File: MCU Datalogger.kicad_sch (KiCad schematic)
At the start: 0 parts

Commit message: Have added required symbols to the schematic sheets.
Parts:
- added BT?: Battery, symbol Device:Battery
- added C? (x5): C, symbol Device:C
- added D? (x2): LED, symbol Device:LED
- added H? (x4): MountingHole, symbol Mechanical:MountingHole
- added R? (x7): R, symbol Device:R
- added U?: DS1337S_, DS1337S_:SOIC127P600X175-8N, symbol DS1337S_:DS1337S_
- added U? (x2): 24LC1025, symbol Memory_EEPROM:24LC1025
- added U?: ATMEGA328P-AU, ATMEGA328P-AU:QFP80P900X900X120-32N, symbol ATMEGA328P-AU:ATMEGA328P-AU
- added Y? (x2): Crystal, symbol Device:Crystal
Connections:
- new net: U?.21 (GND), U?.3 (GND), U?.5 (GND)
- new net: U?.4 (VCC), U?.6 (VCC)
- no-connect marks 0 -> 1
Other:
- added sheet Connectors (connectors.kicad_sch)

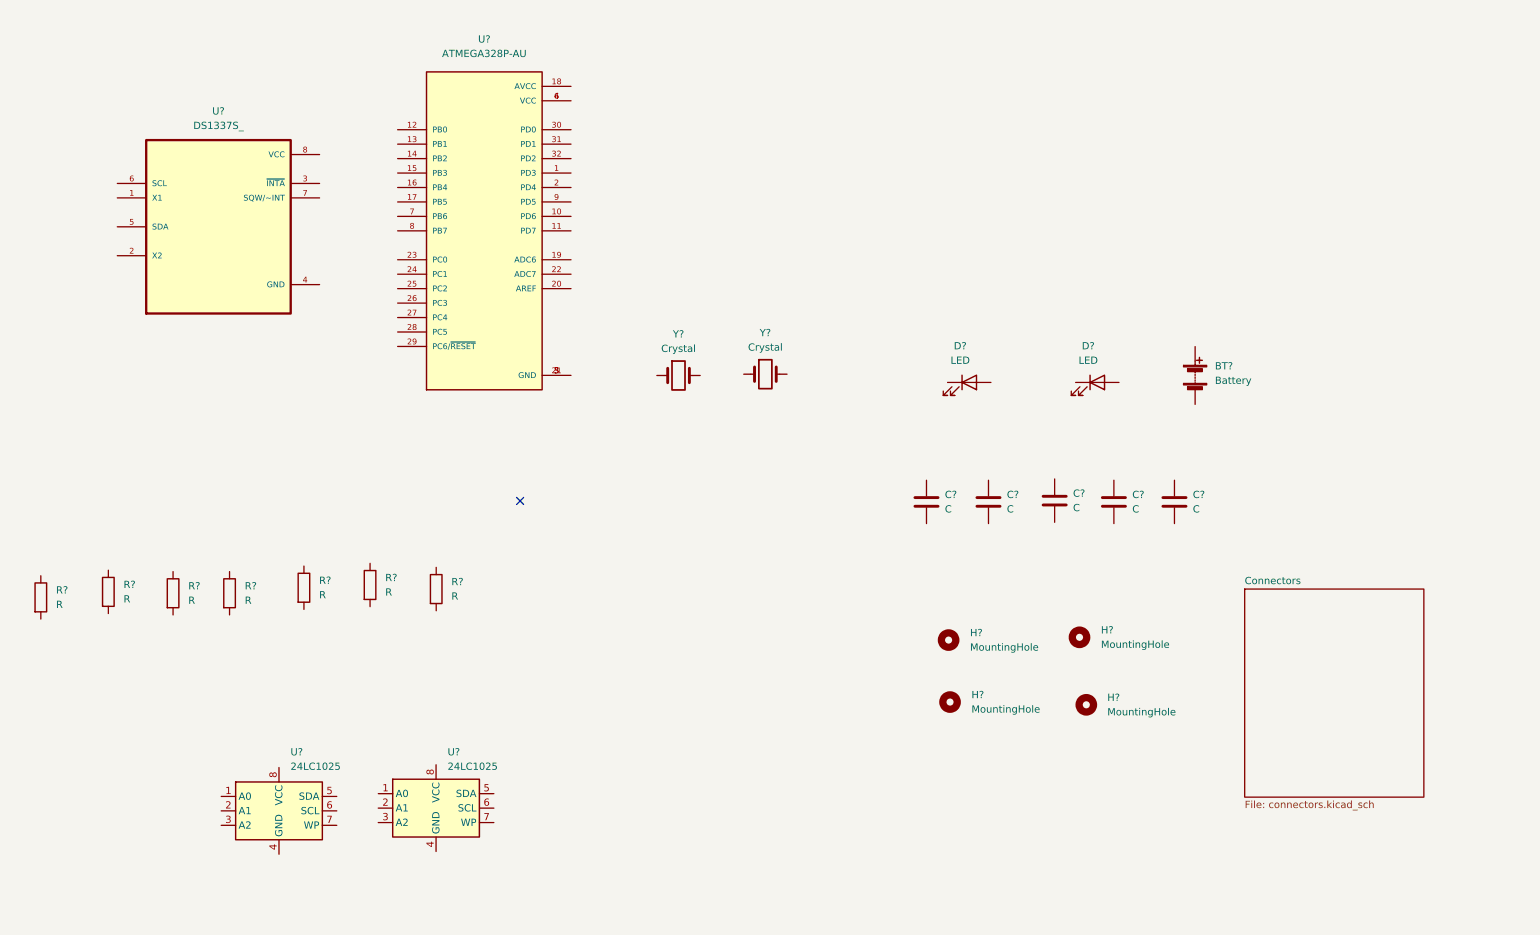
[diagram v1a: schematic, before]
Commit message: Changed locations of symbols (arrange).
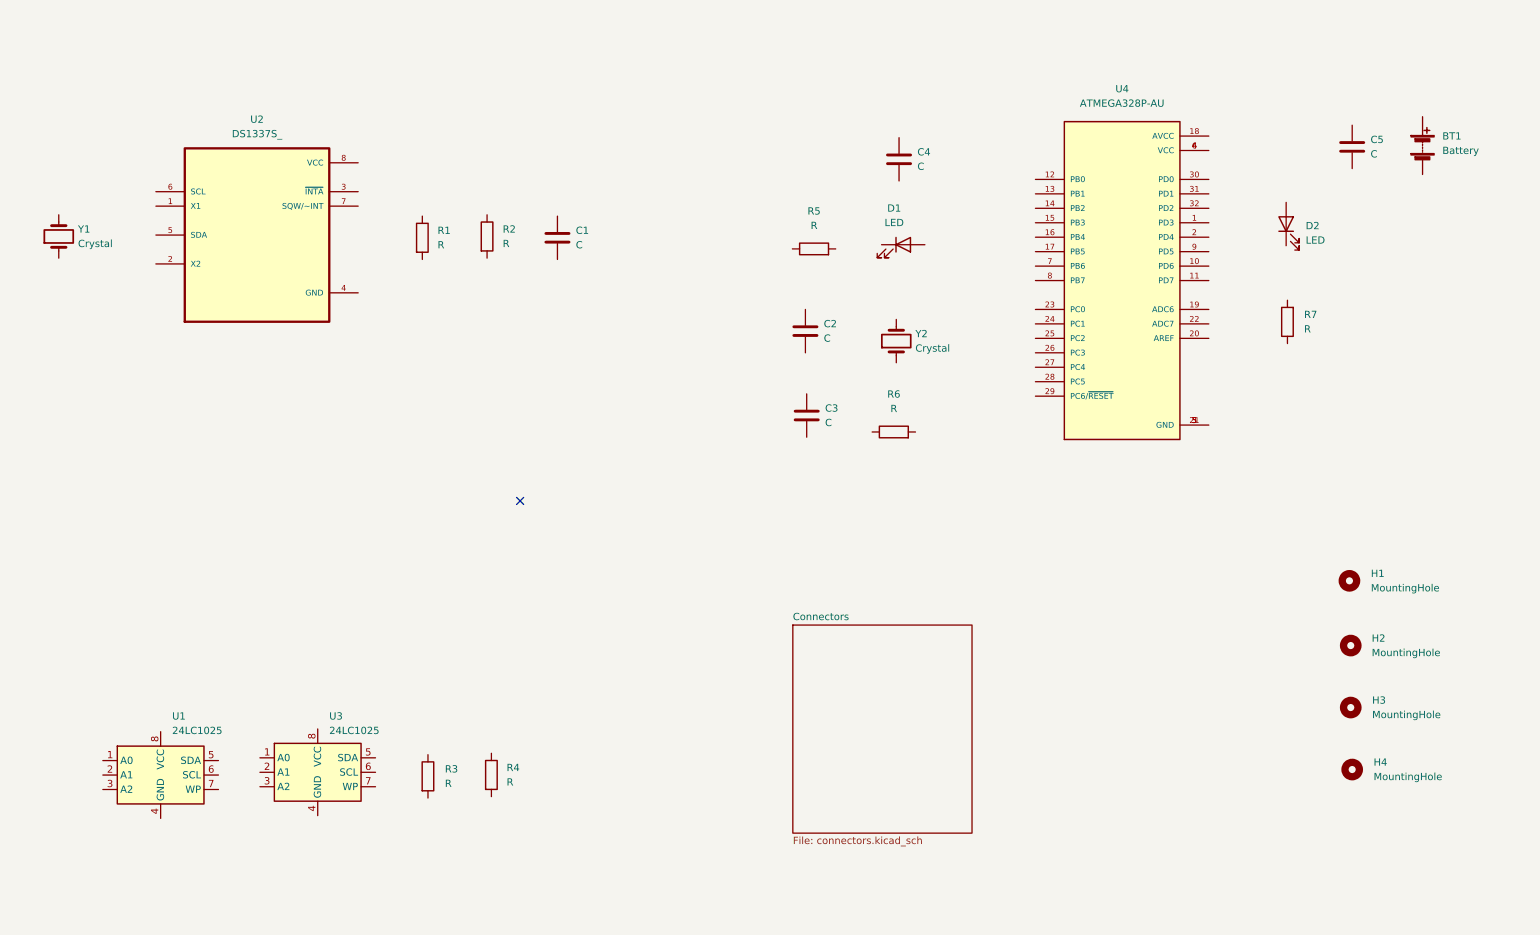
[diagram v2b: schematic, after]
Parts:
- gave numbers to parts that had none: 25
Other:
- moved on the sheet: BT1, C1, C2, C3, C4, C5, D1, D2, H1, H2, H3, H4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

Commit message: Added component values.
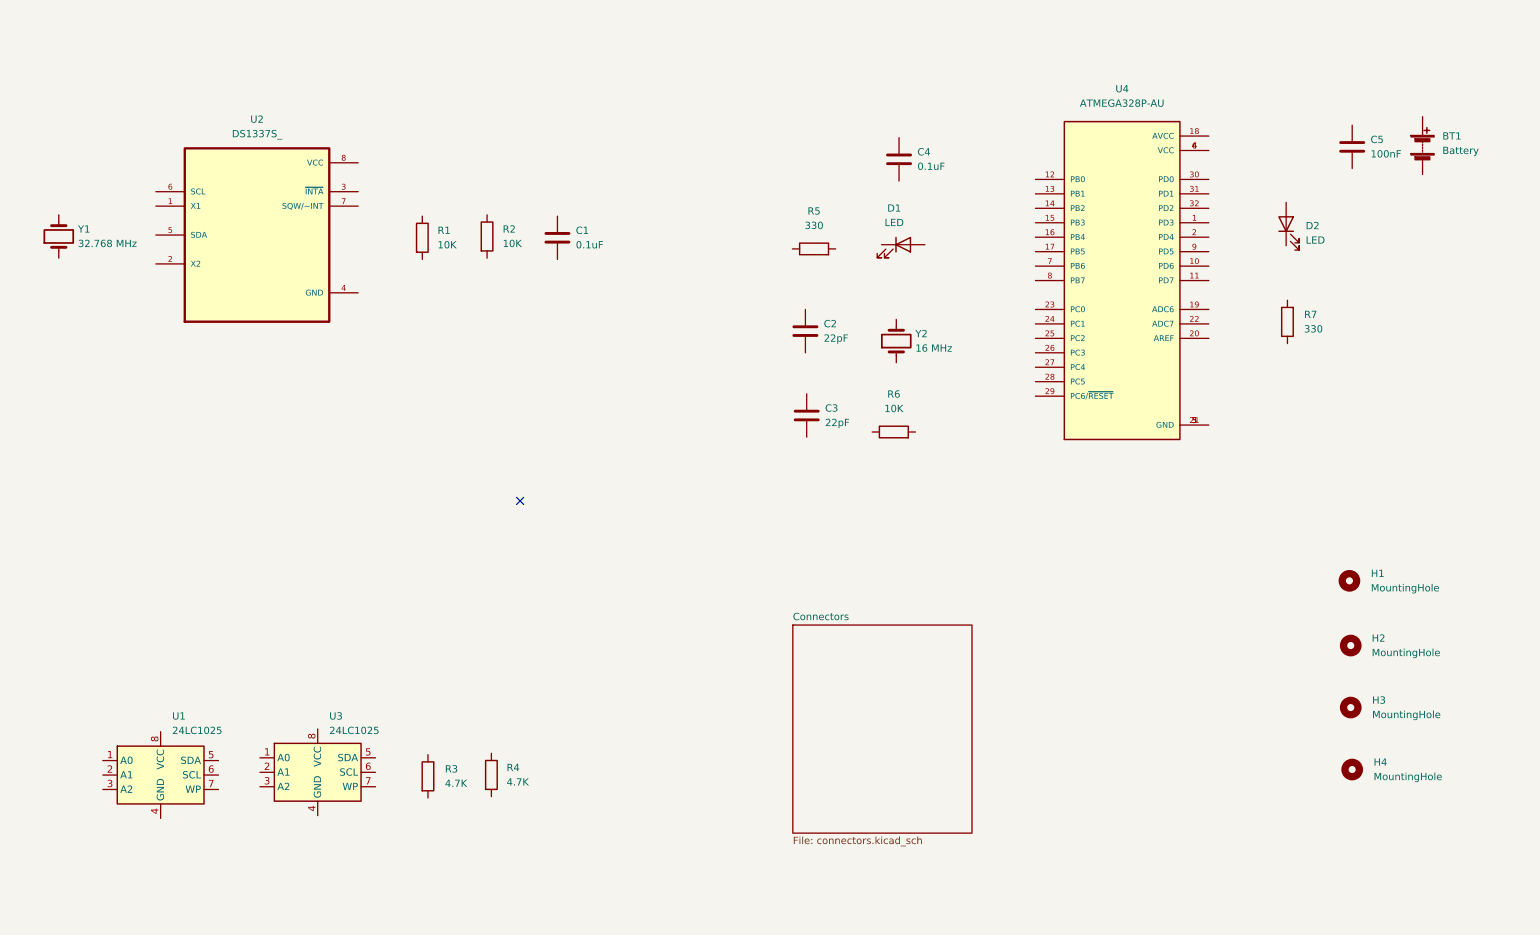
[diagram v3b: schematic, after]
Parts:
- C1, C4: value C -> 0.1uF
- C2, C3: value C -> 22pF
- C5: value C -> 100nF
- R1, R2, R6: value R -> 10K
- R3, R4: value R -> 4.7K
- R5, R7: value R -> 330
- Y1: value Crystal -> 32.768 MHz
- Y2: value Crystal -> 16 MHz
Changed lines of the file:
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@@
       (effects (font (size 1.27 1.27)) (justify left))
     )
-    (property "Value" "C" (id 1) (at 254.1524 39.9287 0)
+    (property "Value" "100nF" (id 1) (at 254.1524 39.9287 0)
       (effects (font (size 1.27 1.27)) (justify left))
     )
@@
       (effects (font (size 1.27 1.27)) (justify left))
     )
-    (property "Value" "R" (id 1) (at 102.2845 150.329 0)
+    (property "Value" "4.7K" (id 1) (at 102.2845 150.329 0)
       (effects (font (size 1.27 1.27)) (justify left))
     )
@@
     (in_bom yes) (on_board yes) (fields_autoplaced)
     (property "Reference" "R5" (id 0) (at 156.337 49.9618 90))
-    (property "Value" "R" (id 1) (at 156.337 52.5018 90))
+    (property "Value" "330" (id 1) (at 156.337 52.5018 90))
     (property "Footprint" "" (id 2) (at 156.337 58.3692 90)
       (effects (font (size 1.27 1.27)) hide)
@@
       (effects (font (size 1.27 1.27)) (justify left))
     )
-    (property "Value" "C" (id 1) (at 114.4524 55.9053 0)
+    (property "Value" "0.1uF" (id 1) (at 114.4524 55.9053 0)
       (effects (font (size 1.27 1.27)) (justify left))
     )
@@
       (effects (font (size 1.27 1.27)) (justify left))
     )
-    (property "Value" "C" (id 1) (at 158.0388 72.3137 0)
+    (property "Value" "22pF" (id 1) (at 158.0388 72.3137 0)
       (effects (font (size 1.27 1.27)) (justify left))
     )
@@
       (effects (font (size 1.27 1.27)) (justify right))
     )
-    (property "Value" "R" (id 1) (at 242.4684 70.6881 0)
+    (property "Value" "330" (id 1) (at 242.4684 70.6881 0)
       (effects (font (size 1.27 1.27)) (justify right))
     )
@@
       (effects (font (size 1.27 1.27)) (justify left))
     )
-    (property "Value" "C" (id 1) (at 174.498 42.1131 0)
+    (property "Value" "0.1uF" (id 1) (at 174.498 42.1131 0)
       (effects (font (size 1.27 1.27)) (justify left))
     )
@@
       (effects (font (size 1.27 1.27)) (justify left))
     )
-    (property "Value" "C" (id 1) (at 158.2674 87.1473 0)
+    (property "Value" "22pF" (id 1) (at 158.2674 87.1473 0)
       (effects (font (size 1.27 1.27)) (justify left))
     )
@@
       (effects (font (size 1.27 1.27)) (justify right))
     )
-    (property "Value" "Crystal" (id 1) (at 26.9494 55.6768 90)
+    (property "Value" "32.768 MHz" (id 1) (at 26.9494 55.6768 90)
       (effects (font (size 1.27 1.27)) (justify right))
     )
@@
       (effects (font (size 1.27 1.27)) (justify right))
     )
-    (property "Value" "Crystal" (id 1) (at 174.1424 74.0663 90)
+    (property "Value" "16 MHz" (id 1) (at 174.1424 74.0663 90)
       (effects (font (size 1.27 1.27)) (justify right))
     )
@@
       (effects (font (size 1.27 1.27)) (justify left))
     )
-    (property "Value" "R" (id 1) (at 101.6 55.6767 0)
+    (property "Value" "10K" (id 1) (at 101.6 55.6767 0)
       (effects (font (size 1.27 1.27)) (justify left))
     )
@@
     (in_bom yes) (on_board yes) (fields_autoplaced)
     (property "Reference" "R6" (id 0) (at 170.3578 82.1436 90))
-    (property "Value" "R" (id 1) (at 170.3578 84.6836 90))
+    (property "Value" "10K" (id 1) (at 170.3578 84.6836 90))
     (property "Footprint" "" (id 2) (at 170.3578 90.551 90)
       (effects (font (size 1.27 1.27)) hide)
@@
       (effects (font (size 1.27 1.27)) (justify left))
     )
-    (property "Value" "R" (id 1) (at 91.44 150.5711 0)
+    (property "Value" "4.7K" (id 1) (at 91.44 150.5711 0)
       (effects (font (size 1.27 1.27)) (justify left))
     )
@@
       (effects (font (size 1.27 1.27)) (justify left))
     )
-    (property "Value" "R" (id 1) (at 90.1446 55.9053 0)
+    (property "Value" "10K" (id 1) (at 90.1446 55.9053 0)
       (effects (font (size 1.27 1.27)) (justify left))
     )
@@
     )
     (path "/3e043e40-a4b6-402b-8bd9-59ccd2f77b77"
-      (reference "C1") (unit 1) (value "C") (footprint "")
+      (reference "C1") (unit 1) (value "0.1uF") (footprint "")
     )
     (path "/4366e5a5-8c8e-4bb5-b500-5758f5731966"
-      (reference "C2") (unit 1) (value "C") (footprint "")
+      (reference "C2") (unit 1) (value "22pF") (footprint "")
     )
     (path "/66e5cbcf-36e0-42bc-8ba1-f5059b7cfc15"
-      (reference "C3") (unit 1) (value "C") (footprint "")
+      (reference "C3") (unit 1) (value "22pF") (footprint "")
     )
     (path "/63f73b7b-4a74-4e91-a39f-8d5f64e14eff"
-      (reference "C4") (unit 1) (value "C") (footprint "")
+      (reference "C4") (unit 1) (value "0.1uF") (footprint "")
     )
     (path "/007d1bf2-b9b2-433c-880e-d6af578e46b6"
-      (reference "C5") (unit 1) (value "C") (footprint "")
+      (reference "C5") (unit 1) (value "100nF") (footprint "")
     )
     (path "/d19902ea-f1a1-4232-8f35-23fa80cf9135"
@@
     )
     (path "/f9104431-c12b-4262-85a4-3fb81a6448ea"
-      (reference "R1") (unit 1) (value "R") (footprint "")
+      (reference "R1") (unit 1) (value "10K") (footprint "")
     )
     (path "/bedc736b-0cbf-45e3-9458-4c80444315d6"
-      (reference "R2") (unit 1) (value "R") (footprint "")
+      (reference "R2") (unit 1) (value "10K") (footprint "")
     )
     (path "/ec0987b2-cb6c-42f0-9b54-c0fd7840ea9e"
-      (reference "R3") (unit 1) (value "R") (footprint "")
+      (reference "R3") (unit 1) (value "4.7K") (footprint "")
     )
     (path "/00958a77-4f8f-4a96-ab98-a4b9e5b70721"
-      (reference "R4") (unit 1) (value "R") (footprint "")
+      (reference "R4") (unit 1) (value "4.7K") (footprint "")
     )
     (path "/33078999-e524-4bc6-9073-409f86087795"
-      (reference "R5") (unit 1) (value "R") (footprint "")
+      (reference "R5") (unit 1) (value "330") (footprint "")
     )
     (path "/e228c171-34d8-44fd-85d8-e988baeda0cc"
-      (reference "R6") (unit 1) (value "R") (footprint "")
+      (reference "R6") (unit 1) (value "10K") (footprint "")
     )
     (path "/4551cc91-103e-45f6-b541-99e46cef476f"
-      (reference "R7") (unit 1) (value "R") (footprint "")
+      (reference "R7") (unit 1) (value "330") (footprint "")
     )
     (path "/d678eccf-31cf-4cbb-9a9c-ab27479686cc"
@@
     )
     (path "/72bd9d08-efdd-44c4-bafc-608226803e30"
-      (reference "Y1") (unit 1) (value "Crystal") (footprint "")
+      (reference "Y1") (unit 1) (value "32.768 MHz") (footprint "")
     )
     (path "/8c9fe14e-7b44-4174-88a8-9c4da9bd0385"
-      (reference "Y2") (unit 1) (value "Crystal") (footprint "")
-    )
-  )
+      (reference "Y2") (unit 1) (value "16 MHz") (footprint "")
+    )
+  )

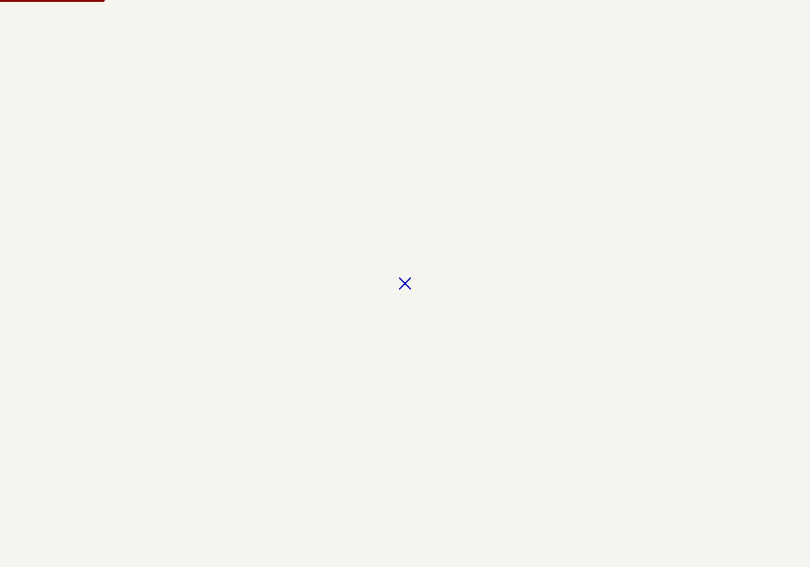
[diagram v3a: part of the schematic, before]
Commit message: Completed symbol-footprint associations.
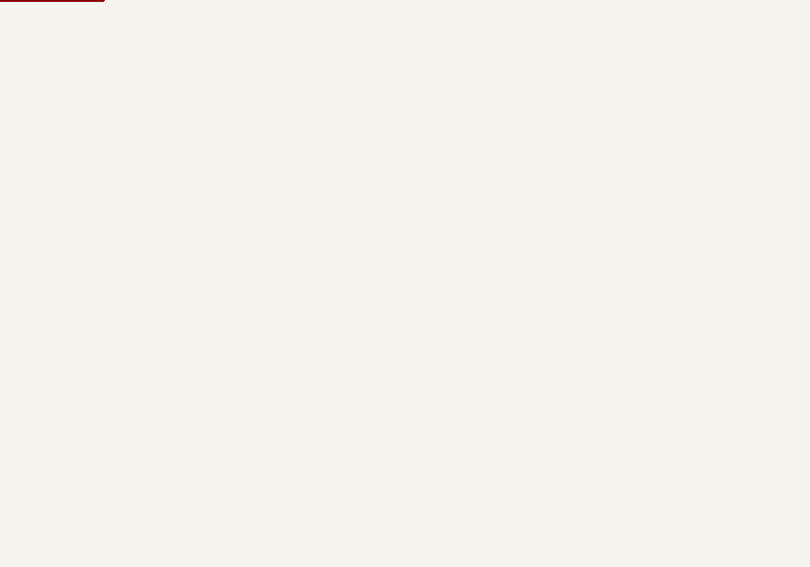
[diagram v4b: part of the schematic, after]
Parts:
- BT1: footprint (none) -> Connector_PinHeader_2.54mm:PinHeader_1x02_P2.54mm_Vertical
- C1, C2, C3, C4, C5: footprint (none) -> Capacitor_SMD:C_0805_2012Metric
- D1, D2: footprint (none) -> LED_SMD:LED_0805_2012Metric
- H1, H2, H3, H4: footprint (none) -> MountingHole:MountingHole_2.1mm
- R1, R2, R3, R4, R5, R6, R7: footprint (none) -> Resistor_SMD:R_0805_2012Metric
- U1, U3: footprint (none) -> Package_SO:SOIC-8_5.23x5.23mm_P1.27mm
- U2: footprint DS1337S_:SOIC127P600X175-8N -> MCU Datalogger:SOIC127P600X175-8N
- U4: footprint ATMEGA328P-AU:QFP80P900X900X120-32N -> MCU Datalogger:QFP80P900X900X120-32N
- Y1, Y2: footprint (none) -> Crystal:Crystal_SMD_5032-2Pin_5.0x3.2mm_HandSoldering
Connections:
- no-connect marks 1 -> 0
